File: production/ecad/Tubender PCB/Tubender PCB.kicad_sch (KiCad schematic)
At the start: 0 parts

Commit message: Added TItle
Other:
- title: (none) -> Generate Fall 2024 - Tubender PCB
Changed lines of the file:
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@@
 	(generator_version "8.0")
 	(paper "A4")
+	(title_block
+		(title "Generate Fall 2024 - Tubender PCB")
+	)
 	(sheet
 		(at 15.875 16.51)

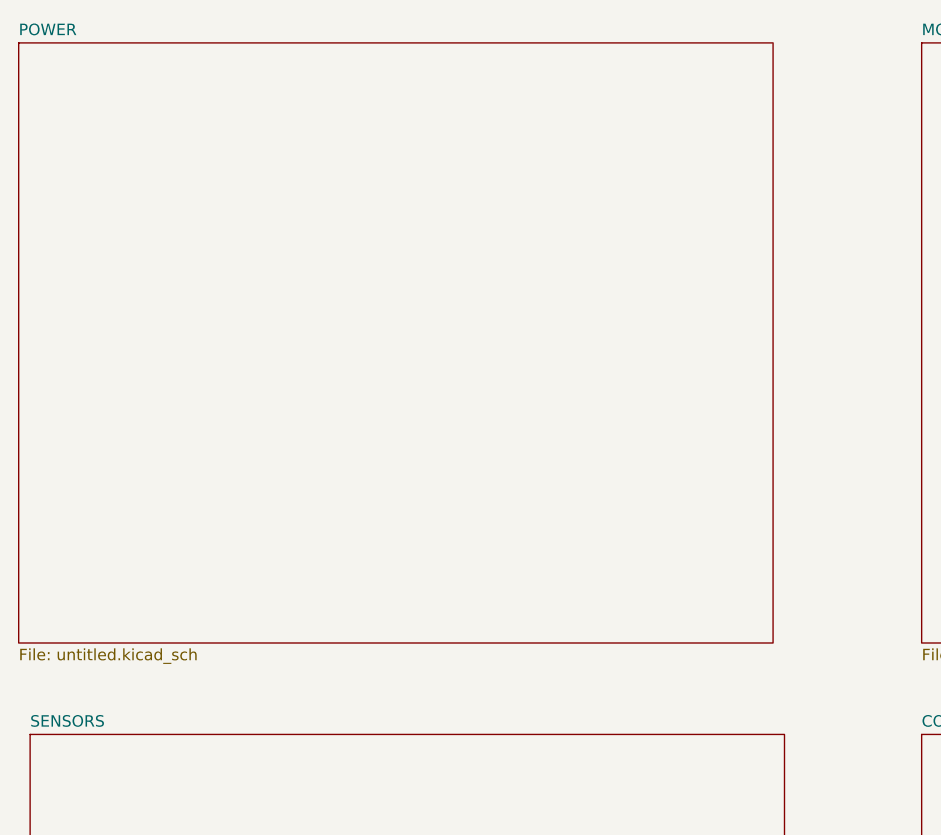
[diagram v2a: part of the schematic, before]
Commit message: added 3.3V buck IC symbol and changed power sheet directory
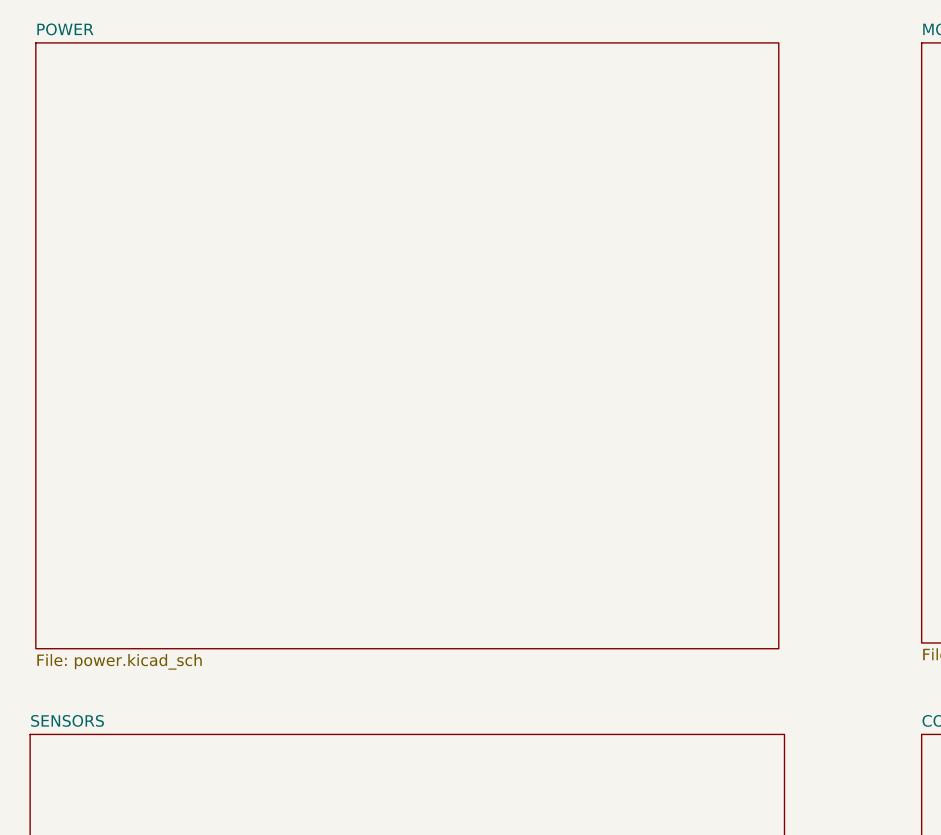
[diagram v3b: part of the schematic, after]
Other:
- sheet POWER: file untitled.kicad_sch -> power.kicad_sch
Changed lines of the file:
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@@
 	)
 	(sheet
-		(at 15.875 16.51)
-		(size 83.82 66.675)
+		(at 17.78 16.51)
+		(size 82.55 67.31)
 		(fields_autoplaced yes)
 		(stroke
@@
 		)
 		(property "Sheetname" "POWER"
-			(at 15.875 15.7984 0)
+			(at 17.78 15.7984 0)
 			(effects
 				(font
@@
 			)
 		)
-		(property "Sheetfile" "untitled.kicad_sch"
-			(at 15.875 83.7696 0)
+		(property "Sheetfile" "power.kicad_sch"
+			(at 17.78 84.4046 0)
 			(effects
 				(font

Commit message: just test push!
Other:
- sheet MOTORS renamed MOTORS & ACTUATORS
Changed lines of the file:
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@@
 			(color 0 0 0 0.0000)
 		)
-		(property "Sheetname" "MOTORS"
+		(property "Sheetname" "MOTORS & ACTUATORS"
 			(at 116.205 15.7984 0)
 			(effects

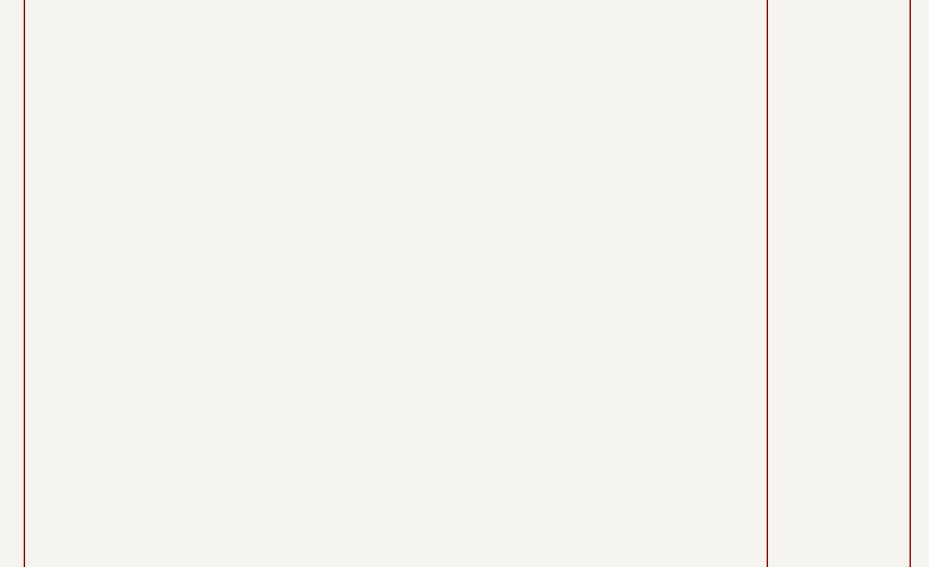
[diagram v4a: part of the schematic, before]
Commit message: Added 3V3 buck circuitry to main branch, added 3V3 label
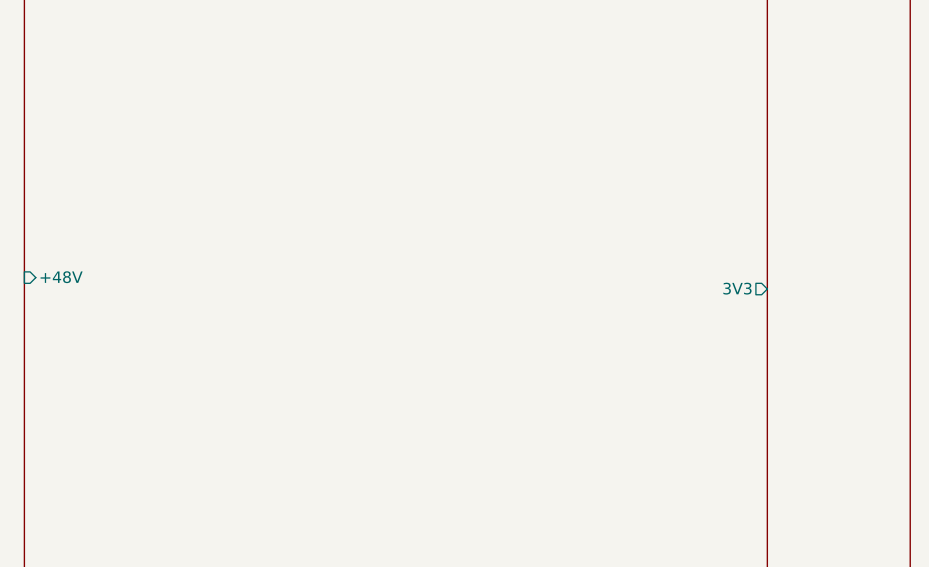
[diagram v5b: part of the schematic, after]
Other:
- sheet POWER ports: added +48V, 3V3; removed none
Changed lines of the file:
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@@
+			)
+		)
+		(pin "3V3" output
+			(at 100.33 50.8 0)
+			(effects
+				(font
+					(size 1.27 1.27)
+				)
+				(justify right)
+			)
+		)
+		(pin "+48V" input
+			(at 17.78 49.53 180)
+			(effects
+				(font
+					(size 1.27 1.27)
+				)
+				(justify left)
 			)
 		)

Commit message: MCU and such
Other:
- sheet CONTROL: file untitled.kicad_sch -> control.kicad_sch
- sheet MOTORS & ACTUATORS: file untitled.kicad_sch -> motors_actuators.kicad_sch
- sheet SENSORS: file untitled.kicad_sch -> sensors.kicad_sch
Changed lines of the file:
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@@
 	)
 	(sheet
-		(at 17.78 16.51)
+		(at 160.02 17.78)
+		(size 82.55 68.58)
+		(fields_autoplaced yes)
+		(stroke
+			(width 0.1524)
+			(type solid)
+		)
+		(fill
+			(color 0 0 0 0.0000)
+		)
+		(property "Sheetname" "MOTORS & ACTUATORS"
+			(at 160.02 17.0684 0)
+			(effects
+				(font
+					(size 1.27 1.27)
+				)
+				(justify left bottom)
+			)
+		)
+		(property "Sheetfile" "motors_actuators.kicad_sch"
+			(at 160.02 86.9446 0)
+			(effects
+				(font
+					(size 1.27 1.27)
+				)
+				(justify left top)
+			)
+		)
+		(instances
+			(project "Tubender PCB"
+				(path "/3e1aedd0-6089-4edb-92c7-0c31da2e7927"
+					(page "3")
+				)
+			)
+		)
+	)
+	(sheet
+		(at 52.07 17.78)
 		(size 82.55 67.31)
 		(fields_autoplaced yes)
@@
 		)
 		(property "Sheetname" "POWER"
-			(at 17.78 15.7984 0)
+			(at 52.07 17.0684 0)
 			(effects
 				(font
@@
 		)
 		(property "Sheetfile" "power.kicad_sch"
-			(at 17.78 84.4046 0)
+			(at 52.07 85.6746 0)
 			(effects
 				(font
@@
 		)
 		(pin "3V3" output
-			(at 100.33 50.8 0)
+			(at 134.62 52.07 0)
 			(effects
 				(font
@@
 		)
 		(pin "+48V" input
-			(at 17.78 49.53 180)
+			(at 52.07 50.8 180)
 			(effects
 				(font
@@
 	)
 	(sheet
-		(at 17.145 93.345)
-		(size 83.82 66.675)
-		(fields_autoplaced yes)
-		(stroke
-			(width 0.1524)
-			(type solid)
-		)
-		(fill
-			(color 0 0 0 0.0000)
-		)
-		(property "Sheetname" "SENSORS"
-			(at 17.145 92.6334 0)
-			(effects
-				(font
-					(size 1.27 1.27)
-				)
-				(justify left bottom)
-			)
-		)
-		(property "Sheetfile" "untitled.kicad_sch"
-			(at 17.145 160.6046 0)
-			(effects
-				(font
-					(size 1.27 1.27)
-				)
-				(justify left top)
-			)
-		)
-		(instances
-			(project "Tubender PCB"
-				(path "/3e1aedd0-6089-4edb-92c7-0c31da2e7927"
-					(page "3")
-				)
-			)
-		)
-	)
-	(sheet
-		(at 116.205 93.345)
-		(size 83.82 66.675)
+		(at 158.75 93.98)
+		(size 85.09 68.58)
 		(fields_autoplaced yes)
 		(stroke
@@
 		)
 		(property "Sheetname" "CONTROL"
-			(at 116.205 92.6334 0)
+			(at 158.75 93.2684 0)
 			(effects
 				(font
@@
 			)
 		)
-		(property "Sheetfile" "untitled.kicad_sch"
-			(at 116.205 160.6046 0)
+		(property "Sheetfile" "control.kicad_sch"
+			(at 158.75 163.1446 0)
 			(effects
 				(font
@@
 	)
 	(sheet
-		(at 116.205 16.51)
-		(size 83.82 66.675)
+		(at 50.8 93.98)
+		(size 83.82 68.58)
 		(fields_autoplaced yes)
 		(stroke
@@
 			(color 0 0 0 0.0000)
 		)
-		(property "Sheetname" "MOTORS & ACTUATORS"
-			(at 116.205 15.7984 0)
+		(property "Sheetname" "SENSORS"
+			(at 50.8 93.2684 0)
 			(effects
 				(font
@@
 			)
 		)
-		(property "Sheetfile" "untitled.kicad_sch"
-			(at 116.205 83.7696 0)
+		(property "Sheetfile" "sensors.kicad_sch"
+			(at 50.8 163.1446 0)
 			(effects
 				(font

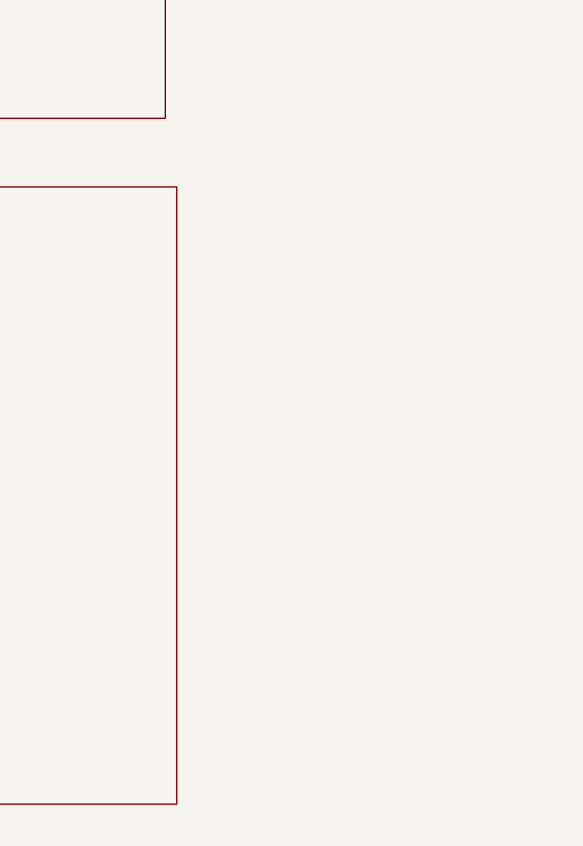
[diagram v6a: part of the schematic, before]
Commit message: Add UI sheet
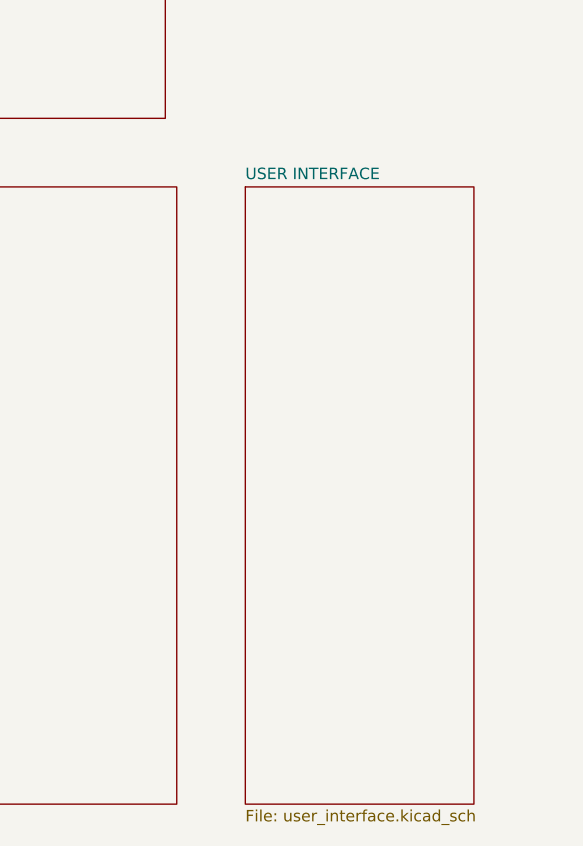
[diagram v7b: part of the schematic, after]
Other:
- added sheet USER INTERFACE (user_interface.kicad_sch)
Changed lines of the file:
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@@
+		)
+	)
+	(sheet
+		(at 251.46 93.98)
+		(size 25.4 68.58)
+		(fields_autoplaced yes)
+		(stroke
+			(width 0.1524)
+			(type solid)
+		)
+		(fill
+			(color 0 0 0 0.0000)
+		)
+		(property "Sheetname" "USER INTERFACE"
+			(at 251.46 93.2684 0)
+			(effects
+				(font
+					(size 1.27 1.27)
+				)
+				(justify left bottom)
+			)
+		)
+		(property "Sheetfile" "user_interface.kicad_sch"
+			(at 251.46 163.1446 0)
+			(effects
+				(font
+					(size 1.27 1.27)
+				)
+				(justify left top)
+			)
+		)
+		(instances
+			(project "Tubender PCB"
+				(path "/3e1aedd0-6089-4edb-92c7-0c31da2e7927"
+					(page "6")
+				)
+			)
 		)
 	)

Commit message: Fixed Button Connectors
All done! Enjoy :)
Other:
- sheet POWER ports: added 12V, 24V, 5V; removed none
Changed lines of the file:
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@@
 	)
 	(sheet
-		(at 160.02 17.78)
-		(size 82.55 68.58)
-		(fields_autoplaced yes)
+		(at 153.67 17.78)
+		(size 77.47 68.58)
 		(stroke
 			(width 0.1524)
@@
 		)
 		(property "Sheetname" "MOTORS & ACTUATORS"
-			(at 160.02 17.0684 0)
-			(effects
-				(font
-					(size 1.27 1.27)
+			(at 171.196 51.308 0)
+			(effects
+				(font
+					(size 2.54 2.54)
+					(thickness 0.508)
+					(bold yes)
 				)
 				(justify left bottom)
@@
 		)
 		(property "Sheetfile" "motors_actuators.kicad_sch"
-			(at 160.02 86.9446 0)
+			(at 153.67 86.9446 0)
 			(effects
 				(font
@@
 	)
 	(sheet
-		(at 52.07 17.78)
-		(size 82.55 67.31)
-		(fields_autoplaced yes)
+		(at 59.69 17.78)
+		(size 74.93 68.58)
 		(stroke
 			(width 0.1524)
@@
 		)
 		(property "Sheetname" "POWER"
-			(at 52.07 17.0684 0)
-			(effects
-				(font
-					(size 1.27 1.27)
+			(at 90.424 52.07 0)
+			(effects
+				(font
+					(size 2.54 2.54)
+					(thickness 0.508)
+					(bold yes)
 				)
 				(justify left bottom)
@@
 		)
 		(property "Sheetfile" "power.kicad_sch"
-			(at 52.07 85.6746 0)
+			(at 59.69 86.9446 0)
 			(effects
 				(font
@@
 		)
 		(pin "3V3" output
-			(at 134.62 52.07 0)
+			(at 134.62 57.15 0)
 			(effects
 				(font
@@
 		)
 		(pin "+48V" input
-			(at 52.07 50.8 180)
+			(at 59.69 50.8 180)
 			(effects
 				(font
@@
 			)
 		)
+		(pin "12V" output
+			(at 134.62 49.53 0)
+			(effects
+				(font
+					(size 1.27 1.27)
+				)
+				(justify right)
+			)
+		)
+		(pin "5V" output
+			(at 134.62 53.34 0)
+			(effects
+				(font
+					(size 1.27 1.27)
+				)
+				(justify right)
+			)
+		)
+		(pin "24V" output
+			(at 134.62 45.72 0)
+			(effects
+				(font
+					(size 1.27 1.27)
+				)
+				(justify right)
+			)
+		)
 		(instances
 			(project "Tubender PCB"
@@
 	)
 	(sheet
-		(at 158.75 93.98)
-		(size 85.09 68.58)
-		(fields_autoplaced yes)
+		(at 106.68 95.25)
+		(size 81.28 68.58)
 		(stroke
 			(width 0.1524)
@@
 		)
 		(property "Sheetname" "CONTROL"
-			(at 158.75 93.2684 0)
-			(effects
-				(font
-					(size 1.27 1.27)
+			(at 137.922 130.556 0)
+			(effects
+				(font
+					(size 2.54 2.54)
+					(thickness 0.508)
+					(bold yes)
 				)
 				(justify left bottom)
@@
 		)
 		(property "Sheetfile" "control.kicad_sch"
-			(at 158.75 163.1446 0)
+			(at 106.68 164.4146 0)
 			(effects
 				(font
@@
 	)
 	(sheet
-		(at 50.8 93.98)
-		(size 83.82 68.58)
-		(fields_autoplaced yes)
+		(at 16.51 95.25)
+		(size 80.01 68.58)
 		(stroke
 			(width 0.1524)
@@
 		)
 		(property "Sheetname" "SENSORS"
-			(at 50.8 93.2684 0)
-			(effects
-				(font
-					(size 1.27 1.27)
+			(at 45.466 130.556 0)
+			(effects
+				(font
+					(size 2.54 2.54)
+					(thickness 0.508)
+					(bold yes)
 				)
 				(justify left bottom)
@@
 		)
 		(property "Sheetfile" "sensors.kicad_sch"
-			(at 50.8 163.1446 0)
+			(at 16.51 164.4146 0)
 			(effects
 				(font
@@
 	)
 	(sheet
-		(at 251.46 93.98)
-		(size 25.4 68.58)
-		(fields_autoplaced yes)
+		(at 198.12 93.98)
+		(size 78.74 68.58)
 		(stroke
 			(width 0.1524)
@@
 		)
 		(property "Sheetname" "USER INTERFACE"
-			(at 251.46 93.2684 0)
-			(effects
-				(font
-					(size 1.27 1.27)
+			(at 221.488 130.556 0)
+			(effects
+				(font
+					(size 2.54 2.54)
+					(thickness 0.508)
+					(bold yes)
 				)
 				(justify left bottom)
@@
 		)
 		(property "Sheetfile" "user_interface.kicad_sch"
-			(at 251.46 163.1446 0)
-			(effects
-				(font
+			(at 198.12 163.1446 0)
+			(effects
+				(font
